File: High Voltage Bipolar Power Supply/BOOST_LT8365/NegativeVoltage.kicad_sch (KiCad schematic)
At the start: 42 parts, among them J4 FCR7350Y, J5 FCR7350B, Q3 FZT757TA, Q5 FZT757TA, U3 LT8365, U4 LM329BZ, U6 LM337_SOT223

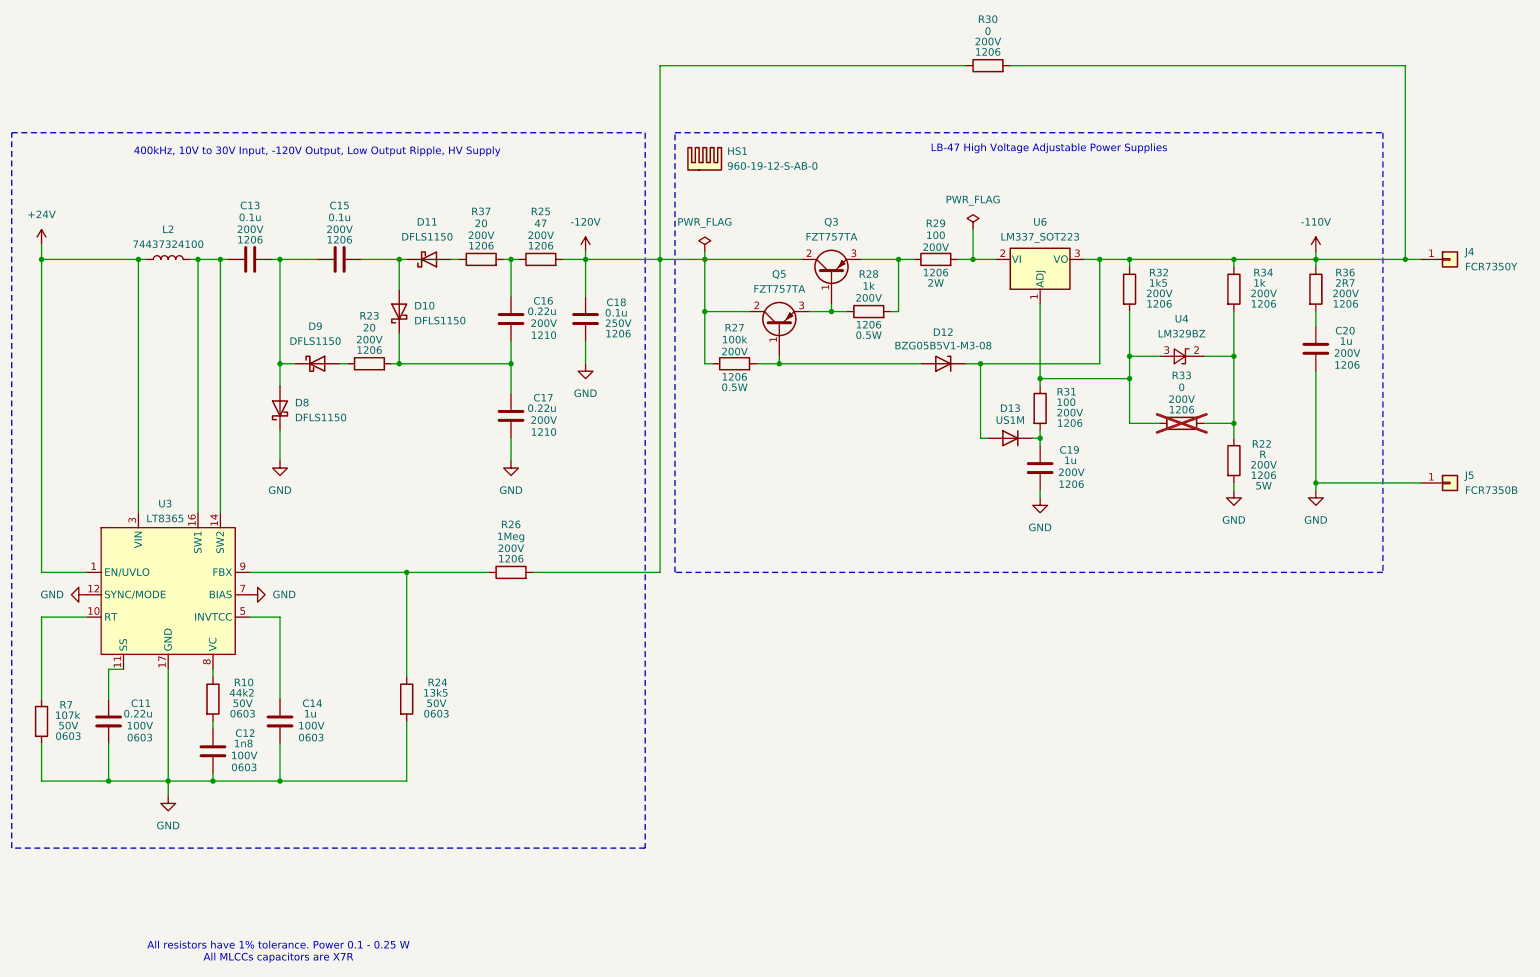
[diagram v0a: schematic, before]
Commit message: Deleted LM317 and LM337 regulator circuits because of current lost on the volateges setup resistors.
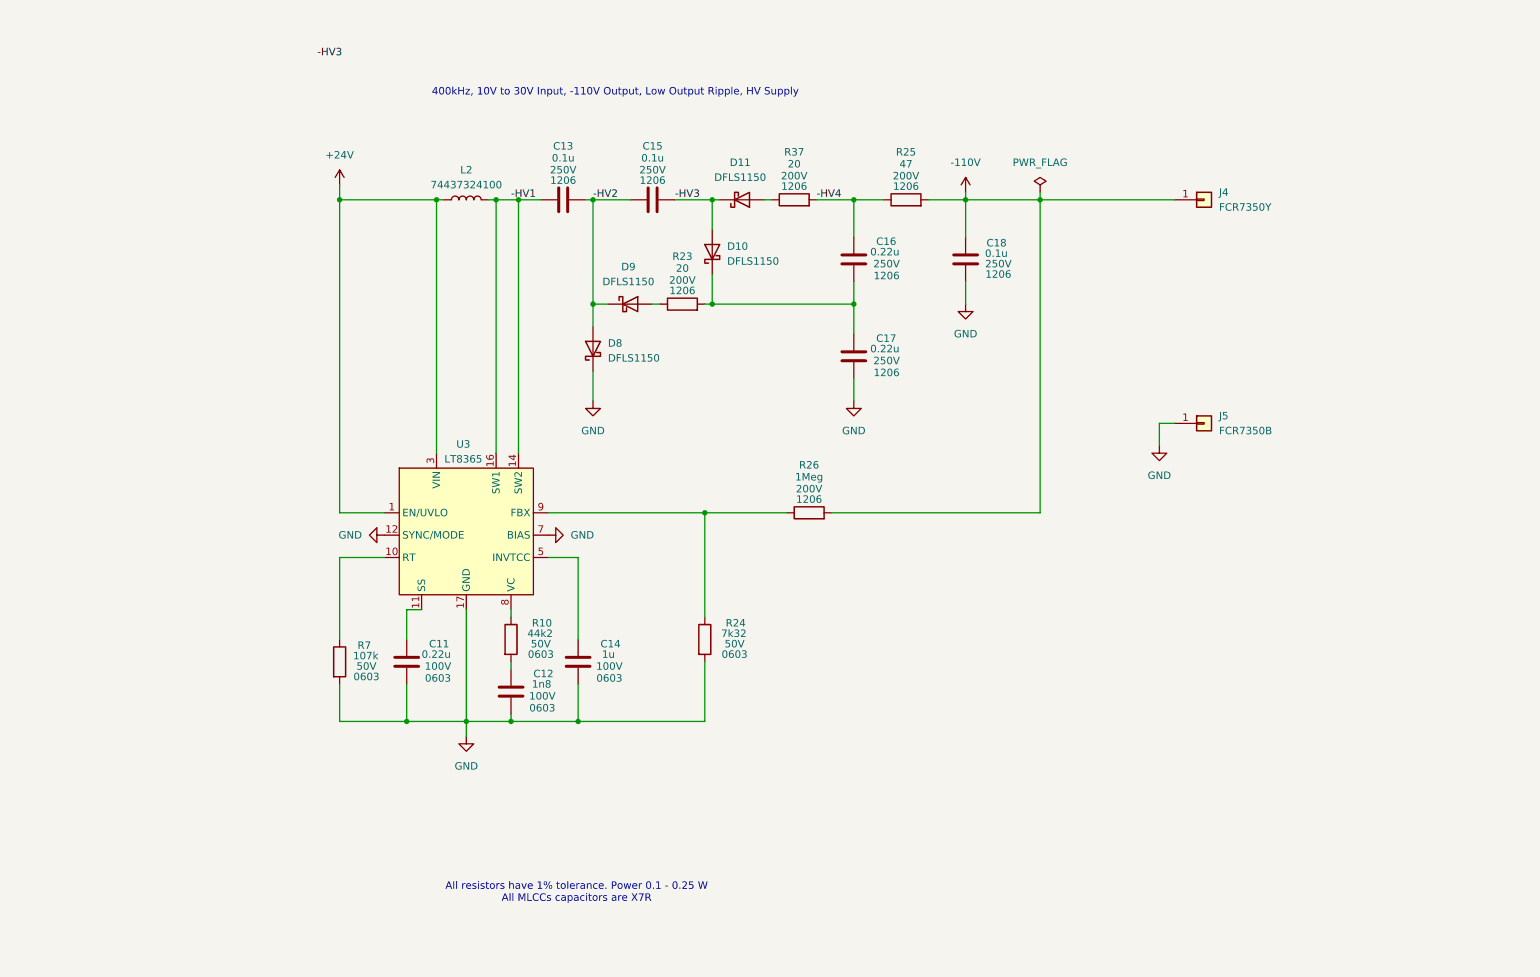
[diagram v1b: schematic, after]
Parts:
- removed C19, C20: 1u, symbol Device:C
- removed D12: BZG05B5V1-M3-08, symbol Device:D_Zener
- removed D13: US1M, Diode_SMD:D_SMA, symbol Diode:US1M
- removed HS1: 960-19-12-S-AB-0, BOOST_LT8365:960-19-12-S-AB-0, symbol Mechanical:Heatsink
- removed Q3, Q5: FZT757TA, symbol Device:Q_PNP_BCE
- removed R22: R, symbol Device:R
- removed R27: 100k, symbol Device:R
- removed R28, R34: 1k, symbol Device:R
- removed R29, R31: 100, symbol Device:R
- removed R30, R33: 0, symbol Device:R
- removed R32: 1k5, symbol Device:R
- removed R36: 2R7, symbol Device:R
- removed U4: LM329BZ, Package_TO_SOT_THT:TO-92_Inline_Horizontal2, symbol Reference_Voltage:LM329xZ
- removed U6: LM337_SOT223, Package_TO_SOT_SMD:SOT-223-3_TabPin2, symbol Regulator_Linear:LM337_SOT223
- C11, C12, C14: footprint (none) -> Capacitor_SMD:C_0603_1608Metric_Pad1.08x0.95mm_HandSolder
- C13, C15: footprint (none) -> Capacitor_SMD:C_1206_3216Metric_Pad1.33x1.80mm_HandSolder; Voltage 200V -> 250V
- C16, C17: footprint (none) -> Capacitor_SMD:C_1206_3216Metric_Pad1.33x1.80mm_HandSolder; Package 1210 -> 1206; Voltage 200V -> 250V
- C18: footprint (none) -> Capacitor_SMD:C_1206_3216Metric_Pad1.33x1.80mm_HandSolder
- D10, D11, D8, D9: footprint (none) -> Diode_SMD:D_PowerDI-123
- R10, R7: footprint (none) -> Resistor_SMD:R_0603_1608Metric_Pad0.98x0.95mm_HandSolder
- R23, R25, R26, R37: footprint (none) -> Resistor_SMD:R_1206_3216Metric_Pad1.30x1.75mm_HandSolder
- R24: value 13k5 -> 7k32; footprint (none) -> Resistor_SMD:R_0603_1608Metric_Pad0.98x0.95mm_HandSolder
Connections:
- net -120V is gone; now on net -110V: C18.1, R25.2, R26.2
- net -HV4: now reaches C16.1, R25.1, R37.2
- net -HV1: now reaches C13.1, L2.2, U3.14 (SW2), U3.16 (SW1)
- net -HV2: now reaches C13.2, C15.1, D8.2 (A), D9.1 (K)
- net -HV3: now reaches C15.2, D10.2 (A), D11.1 (K)
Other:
- note added: "400kHz, 10V to 30V Input, -110V Output, Low Output Ripple, HV Supply"
- note removed: "400kHz, 10V to 30V Input, -120V Output, Low Output Ripple, HV Supply"
- note removed: "LB-47 High Voltage Adjustable Power Supplies"
- moved on the sheet: C11, C12, C13, C14, C15, C16, C17, C18, D10, D11, D8, D9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

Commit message: BOOST_LT8365 : PCB layout
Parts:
- J4, J5: footprint (none) -> BOOST_LT8365:S16N-PC
- L2: footprint (none) -> BOOST_LT8365:74437324100
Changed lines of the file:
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@@
-		)
-	)
-	(label "-HV3"
-		(at 76.2 25.4 0)
-		(fields_autoplaced yes)
-		(effects
-			(font
-				(size 1.27 1.27)
-			)
-			(justify left bottom)
 		)
 	)
@@
 			)
 		)
-		(property "Footprint" ""
+		(property "Footprint" "BOOST_LT8365:74437324100"
 			(at 101.6 49.53 0)
 			(effects
@@
 			)
 		)
-		(property "Footprint" ""
+		(property "Footprint" "BOOST_LT8365:S16N-PC"
 			(at 227.33 87.63 0)
 			(effects
@@
 			)
 		)
-		(property "Footprint" ""
+		(property "Footprint" "BOOST_LT8365:S16N-PC"
 			(at 227.33 49.53 0)
 			(effects
